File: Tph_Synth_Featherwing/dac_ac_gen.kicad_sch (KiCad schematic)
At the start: 10 parts, among them U4 MCP4728

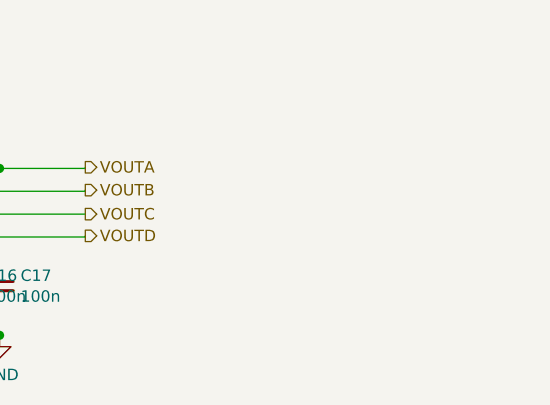
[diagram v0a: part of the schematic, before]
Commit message: Add Qwiic connector to design
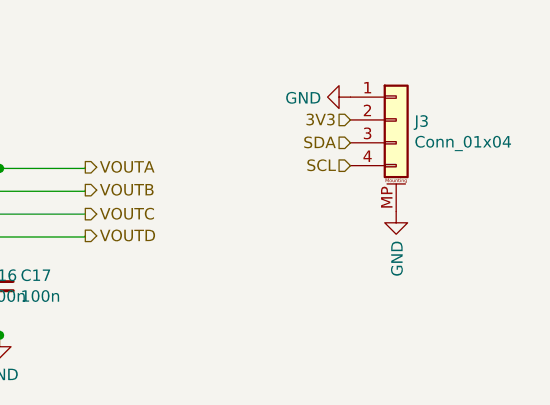
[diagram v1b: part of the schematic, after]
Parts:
- added J3: Conn_01x04, Connector_JST:JST_SH_SM04B-SRSS-TB_1x04-1MP_P1.00mm_Horizontal, symbol Connector_Generic_MountingPin:Conn_01x04_MountingPin
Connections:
- net +3V3: now also J3.2 (Pin_2)
- net GND: now also J3.1 (Pin_1), J3.MP (MountPin)
- net SCL: now also J3.4 (Pin_4)
- net SDA: now also J3.3 (Pin_3)
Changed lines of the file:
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@@
     (effects (font (size 1.27 1.27)) (justify left))
+  )
+  (hierarchical_label "3V3" (shape input) (at 170.18 77.6732 180)
+    (effects (font (size 1.27 1.27)) (justify right))
+  )
+  (hierarchical_label "SDA" (shape input) (at 170.18 80.2132 180)
+    (effects (font (size 1.27 1.27)) (justify right))
+  )
+  (hierarchical_label "SCL" (shape input) (at 170.18 82.7532 180)
+    (effects (font (size 1.27 1.27)) (justify right))
   )
   (symbol (lib_id "Connector:TestPoint") (at 72.644 88.138 90) (unit 1)
@@
     )
   )
+  (symbol (lib_id "power:GND") (at 170.18 75.1332 270) (unit 1)
+    (in_bom yes) (on_board yes)
+    (property "Reference" "#PWR?" (id 0) (at 163.83 75.1332 0)
+      (effects (font (size 1.27 1.27)) hide)
+    )
+    (property "Value" "GND" (id 1) (at 166.9288 75.2602 90)
+      (effects (font (size 1.27 1.27)) (justify right))
+    )
+    (property "Footprint" "" (id 2) (at 170.18 75.1332 0)
+      (effects (font (size 1.27 1.27)) hide)
+    )
+    (property "Datasheet" "" (id 3) (at 170.18 75.1332 0)
+      (effects (font (size 1.27 1.27)) hide)
+    )
+  )
+  (symbol (lib_id "power:GND") (at 175.26 87.8332 0) (unit 1)
+    (in_bom yes) (on_board yes)
+    (property "Reference" "#PWR0104" (id 0) (at 175.26 94.1832 0)
+      (effects (font (size 1.27 1.27)) hide)
+    )
+    (property "Value" "GND" (id 1) (at 175.387 91.0844 90)
+      (effects (font (size 1.27 1.27)) (justify right))
+    )
+    (property "Footprint" "" (id 2) (at 175.26 87.8332 0)
+      (effects (font (size 1.27 1.27)) hide)
+    )
+    (property "Datasheet" "" (id 3) (at 175.26 87.8332 0)
+      (effects (font (size 1.27 1.27)) hide)
+    )
+  )
   (symbol (lib_id "Device:R_Small") (at 70.739 79.756 0) (unit 1)
     (in_bom yes) (on_board yes)
@@
     )
   )
+  (symbol (lib_id "Connector_Generic_MountingPin:Conn_01x04_MountingPin") (at 175.26 77.6732 0) (unit 1)
+    (in_bom yes) (on_board yes)
+    (property "Reference" "J3" (id 0) (at 177.2921 77.8446 0)
+      (effects (font (size 1.27 1.27)) (justify left))
+    )
+    (property "Value" "Conn_01x04" (id 1) (at 177.2921 80.1433 0)
+      (effects (font (size 1.27 1.27)) (justify left))
+    )
+    (property "Footprint" "Connector_JST:JST_SH_SM04B-SRSS-TB_1x04-1MP_P1.00mm_Horizontal" (id 2) (at 175.26 77.6732 0)
+      (effects (font (size 1.27 1.27)) hide)
+    )
+    (property "Datasheet" "~" (id 3) (at 175.26 77.6732 0)
+      (effects (font (size 1.27 1.27)) hide)
+    )
+  )
   (symbol (lib_id "Analog_DAC:MCP4728") (at 104.394 85.598 0) (unit 1)
     (in_bom yes) (on_board yes)
@@
     )
   )
+  (sheet_instances
+    (path "" (page "1"))
+  )
+  (symbol_instances
+    (path "/00000000-0000-0000-0000-00005deccb6b" (reference "#PWR03") (unit 1))
+    (path "/00000000-0000-0000-0000-00005deccddc" (reference "#PWR04") (unit 1))
+    (path "/00000000-0000-0000-0000-00005df82c9c" (reference "#PWR019") (unit 1))
+    (path "/00000000-0000-0000-0000-00005e357714" (reference "#PWR0101") (unit 1))
+    (path "/7fb48a19-c9b9-434f-8c8f-f93783d57d2c" (reference "#PWR0102") (unit 1))
+    (path "/00000000-0000-0000-0000-00005deccadb" (reference "C13") (unit 1))
+    (path "/00000000-0000-0000-0000-00005df8058e" (reference "C14") (unit 1))
+    (path "/00000000-0000-0000-0000-00005df805ce" (reference "C15") (unit 1))
+    (path "/00000000-0000-0000-0000-00005df805f6" (reference "C16") (unit 1))
+    (path "/00000000-0000-0000-0000-00005df80626" (reference "C17") (unit 1))
+    (path "/f2bd2228-639a-485c-88f1-1293787ec652" (reference "J1") (unit 1))
+    (path "/00000000-0000-0000-0000-00005decea02" (reference "R16") (unit 1))
+    (path "/00000000-0000-0000-0000-00005dece9c2" (reference "R17") (unit 1))
+    (path "/00000000-0000-0000-0000-00005decf0bd" (reference "TP6") (unit 1))
+    (path "/00000000-0000-0000-0000-00005decf142" (reference "TP7") (unit 1))
+    (path "/00000000-0000-0000-0000-00005dcbf8fe" (reference "U4") (unit 1))
+  )
 )

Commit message: Improve/update silk screen
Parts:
- J3: manf# (none) -> SM04B-SRSS-TB(LF)(SN)
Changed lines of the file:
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@@
+      (effects (font (size 1.27 1.27)) hide)
+    )
+    (property "manf#" "SM04B-SRSS-TB(LF)(SN)" (id 4) (at 175.26 77.6732 0)
       (effects (font (size 1.27 1.27)) hide)
     )
